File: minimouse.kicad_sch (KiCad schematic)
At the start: 0 parts

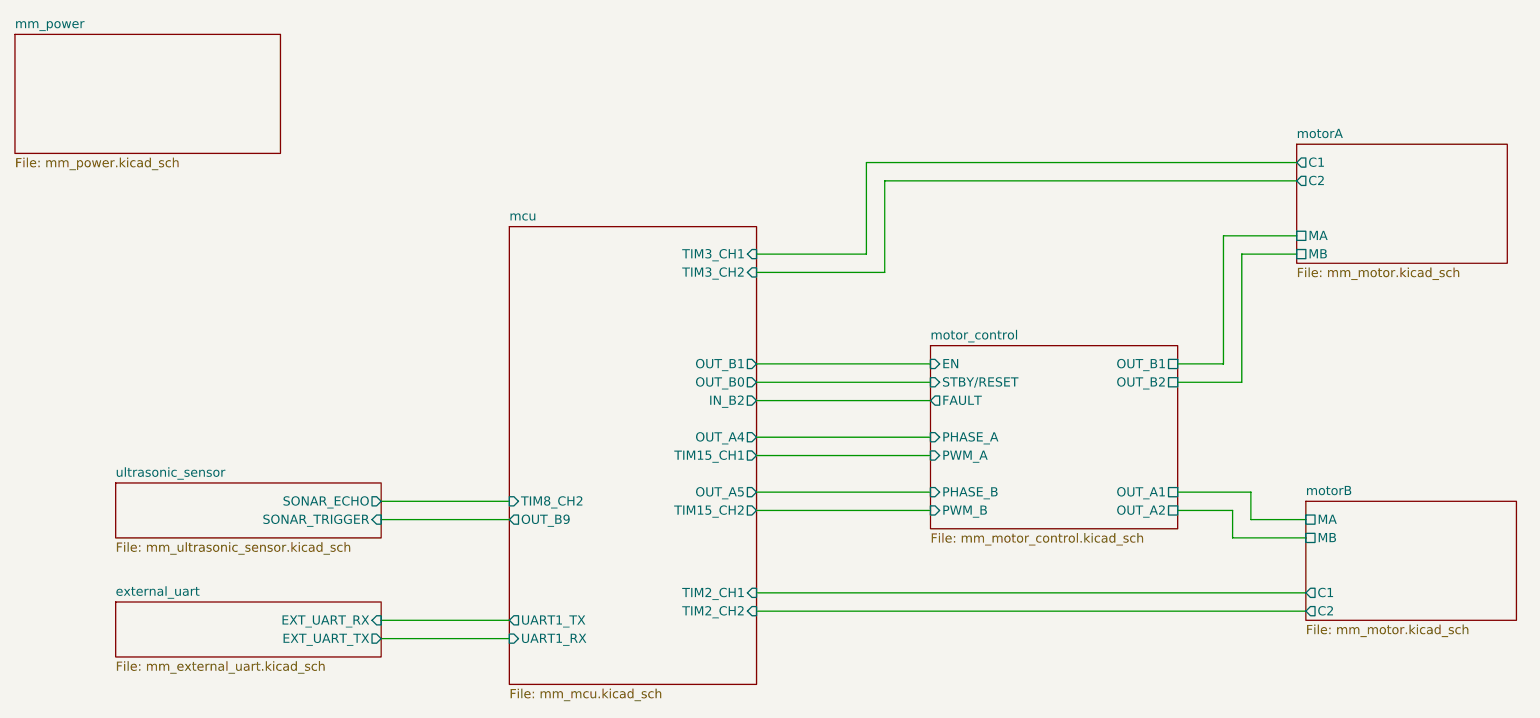
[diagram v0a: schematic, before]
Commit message: ended PCB + added reverse voltage protection
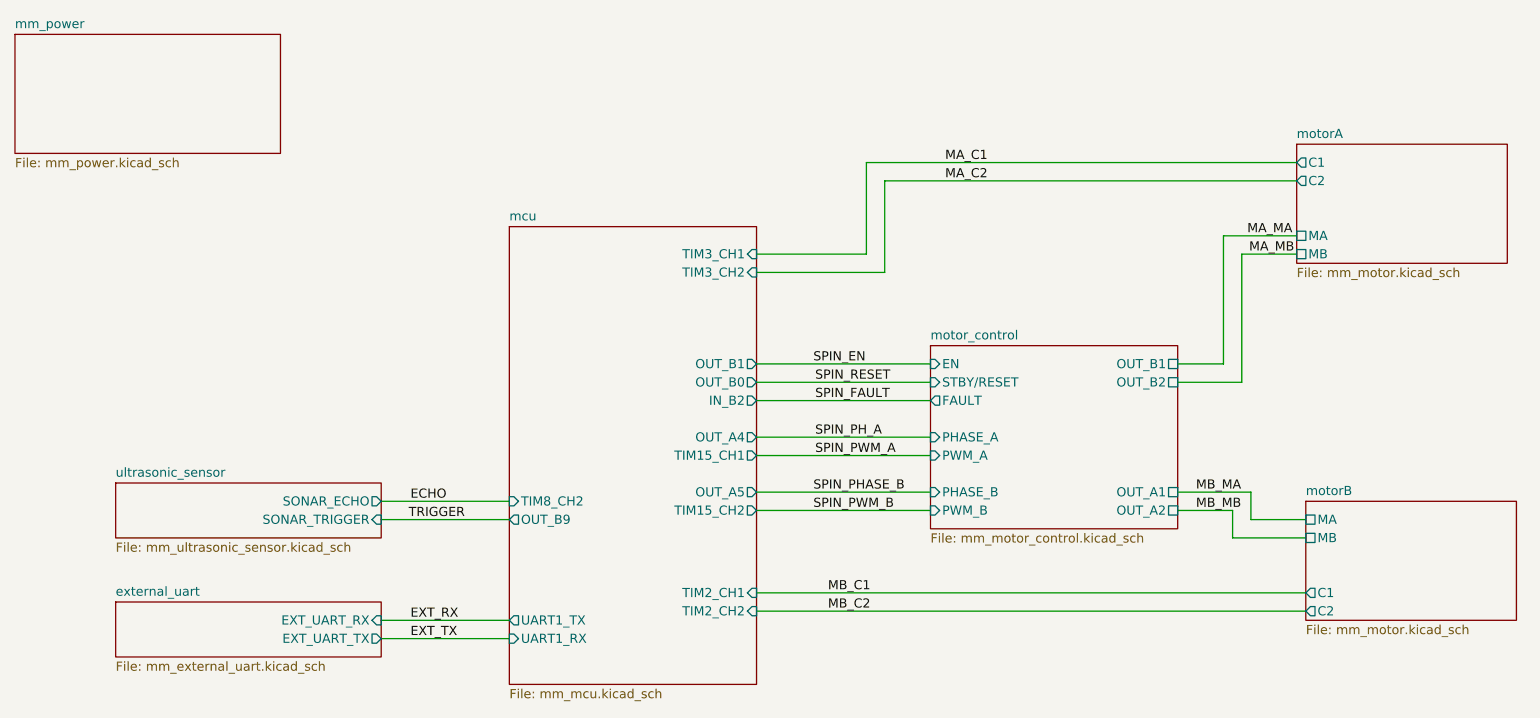
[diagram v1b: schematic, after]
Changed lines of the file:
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@@
     (stroke (width 0) (type default))
+  )
+  (label "ECHO" (at 91.694 91.44 0) (fields_autoplaced)
+    (effects (font (size 1.27 1.27)) (justify left bottom))
+  )
+  (label "MB_MB" (at 200.66 92.71 0) (fields_autoplaced)
+    (effects (font (size 1.27 1.27)) (justify left bottom))
+  )
+  (label "MB_MA" (at 200.66 90.17 0) (fields_autoplaced)
+    (effects (font (size 1.27 1.27)) (justify left bottom))
+  )
+  (label "TRIGGER" (at 91.44 93.98 0) (fields_autoplaced)
+    (effects (font (size 1.27 1.27)) (justify left bottom))
+  )
+  (label "SPIN_FAULT" (at 147.828 77.47 0) (fields_autoplaced)
+    (effects (font (size 1.27 1.27)) (justify left bottom))
+  )
+  (label "SPIN_PH_A" (at 147.828 82.55 0) (fields_autoplaced)
+    (effects (font (size 1.27 1.27)) (justify left bottom))
+  )
+  (label "MB_C2" (at 149.606 106.68 0) (fields_autoplaced)
+    (effects (font (size 1.27 1.27)) (justify left bottom))
+  )
+  (label "MA_C1" (at 165.862 44.45 0) (fields_autoplaced)
+    (effects (font (size 1.27 1.27)) (justify left bottom))
+  )
+  (label "SPIN_PWM_B" (at 147.574 92.71 0) (fields_autoplaced)
+    (effects (font (size 1.27 1.27)) (justify left bottom))
+  )
+  (label "MA_MB" (at 208.026 57.15 0) (fields_autoplaced)
+    (effects (font (size 1.27 1.27)) (justify left bottom))
+  )
+  (label "EXT_TX" (at 91.694 110.49 0) (fields_autoplaced)
+    (effects (font (size 1.27 1.27)) (justify left bottom))
+  )
+  (label "EXT_RX" (at 91.694 107.95 0) (fields_autoplaced)
+    (effects (font (size 1.27 1.27)) (justify left bottom))
+  )
+  (label "SPIN_EN" (at 147.574 72.39 0) (fields_autoplaced)
+    (effects (font (size 1.27 1.27)) (justify left bottom))
+  )
+  (label "SPIN_PHASE_B" (at 147.574 90.17 0) (fields_autoplaced)
+    (effects (font (size 1.27 1.27)) (justify left bottom))
+  )
+  (label "MA_C2" (at 165.862 46.99 0) (fields_autoplaced)
+    (effects (font (size 1.27 1.27)) (justify left bottom))
+  )
+  (label "SPIN_RESET" (at 147.828 74.93 0) (fields_autoplaced)
+    (effects (font (size 1.27 1.27)) (justify left bottom))
+  )
+  (label "MB_C1" (at 149.606 104.14 0) (fields_autoplaced)
+    (effects (font (size 1.27 1.27)) (justify left bottom))
+  )
+  (label "MA_MA" (at 207.772 54.61 0) (fields_autoplaced)
+    (effects (font (size 1.27 1.27)) (justify left bottom))
+  )
+  (label "SPIN_PWM_A" (at 147.828 85.09 0) (fields_autoplaced)
+    (effects (font (size 1.27 1.27)) (justify left bottom))
   )
   (sheet (at 163.83 69.85) (size 34.29 25.4) (fields_autoplaced)
